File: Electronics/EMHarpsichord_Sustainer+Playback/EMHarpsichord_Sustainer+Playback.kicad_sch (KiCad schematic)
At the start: 47 parts, among them J1 Conn_01x03_Male, J2 Conn_01x04_Male, J3 Conn_01x03_Male, U1 ITR20403, U2 NE5532, U3 PAM8406D

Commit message: Reorganizing and Naming files
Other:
- note added: "As of Aug 29 2023: NE5532 on JLCPCB: $0.2116 (<-ended up using this) NE5532 on Digikey: $0.5400 NE5532 on Mouser: $0.5400 LM358 on JLCPCB: $0.4200 LM358 on Digikey:$ $0.400 LM358 on Mouser: $0.4200"
- note removed: "As of Aug 29 2023: NE5532 on JLCPCB: $0.2116 NE5532 on Digikey: $0.5400 NE5532 on Mouser: $0.5400 LM358 on JLCPCB: $0.4200 LM358 on Digikey:$ $0.400 LM358 on Mouser: $0.4200"
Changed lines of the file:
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@@
     (effects (font (size 1.27 1.27)) (justify left bottom))
   )
-  (text "As of Aug 29 2023:\nNE5532 on JLCPCB: $0.2116\nNE5532 on Digikey: $0.5400\nNE5532 on Mouser: $0.5400\nLM358 on JLCPCB: $0.4200\nLM358 on Digikey:$ $0.400\nLM358 on Mouser: $0.4200"
-    (at 20.574 39.116 0)
+  (text "As of Aug 29 2023:\nNE5532 on JLCPCB: $0.2116 (<-ended up using this)\nNE5532 on Digikey: $0.5400\nNE5532 on Mouser: $0.5400\nLM358 on JLCPCB: $0.4200\nLM358 on Digikey:$ $0.400\nLM358 on Mouser: $0.4200"
+    (at 20.574 48.26 0)
     (effects (font (size 1.27 1.27)) (justify left bottom))
   )

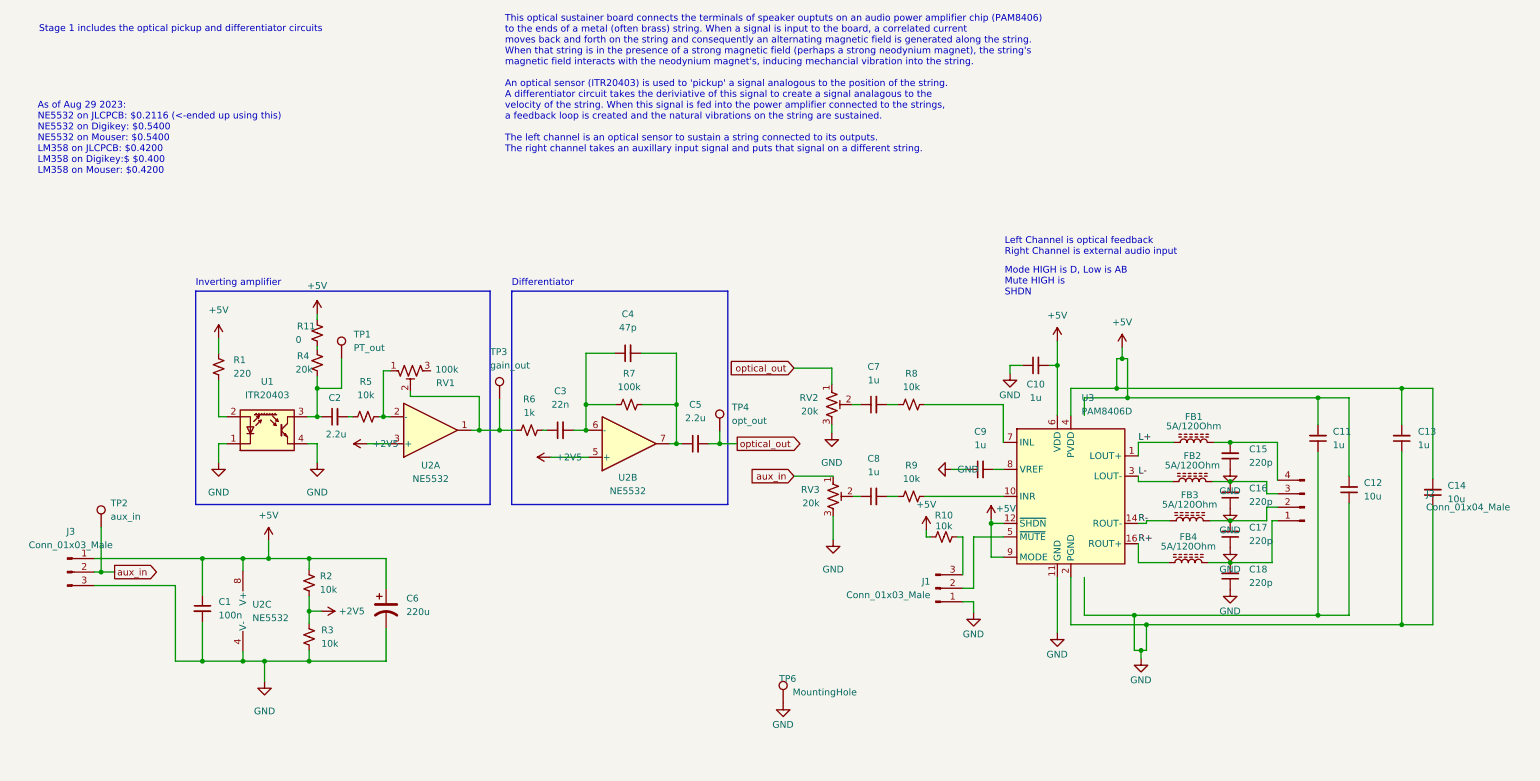
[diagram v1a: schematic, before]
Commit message: More tidying files and adding comments to schematics
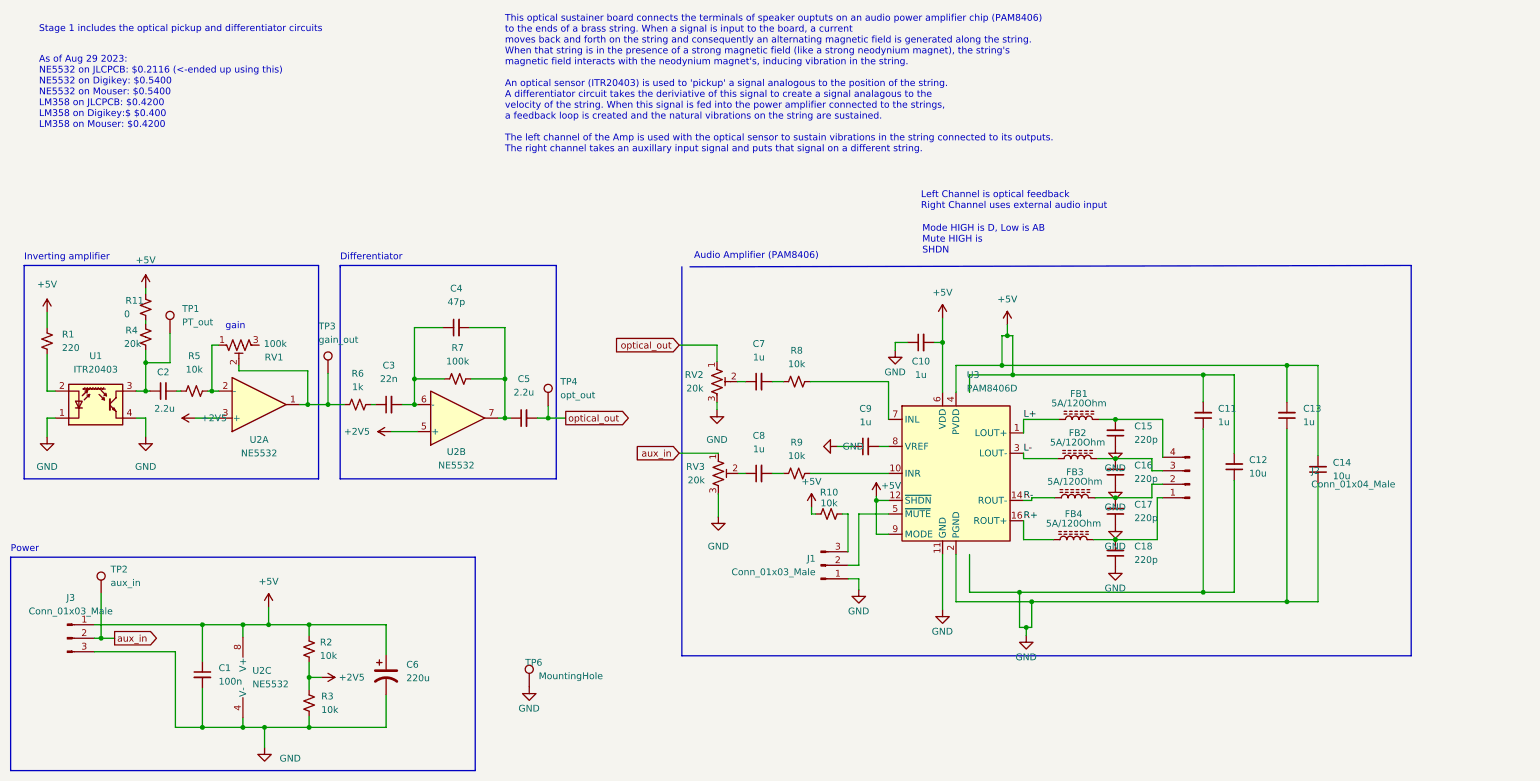
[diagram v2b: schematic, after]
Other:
- note added: "Audio Amplifier (PAM8406)"
- note added: "Left Channel is optical feedback Right Channel uses external audio input"
- note added: "Power"
- note added: "This optical sustainer board connects the terminals of speaker ouptuts on an audio power amplifier chip (PAM8406) to the ends of a brass string. When a signal is input to the board, a current moves back and forth on the string and consequently an alternating magnetic field is generated along the string. When that string is in the presence of a strong magnetic field (like a strong neodynium magnet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"
- note added: "gain"
- note removed: "Left Channel is optical feedback Right Channel is external audio input"
- note removed: "This optical sustainer board connects the terminals of speaker ouptuts on an audio power amplifier chip (PAM8406) to the ends of a metal (often brass) string. When a signal is input to the board, a correlated current moves back and forth on the string and consequently an alternating magnetic field is generated along the string. When that string is in the presence of a strong magnetic field (perha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"
- title: (none) -> EM Harpsichord Sustainer + Playback Board
- moved on the sheet: C1, C10, C11, C12, C13, C14, C15, C16, C17, C18, C2, C3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
